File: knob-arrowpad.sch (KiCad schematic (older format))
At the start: 14 parts

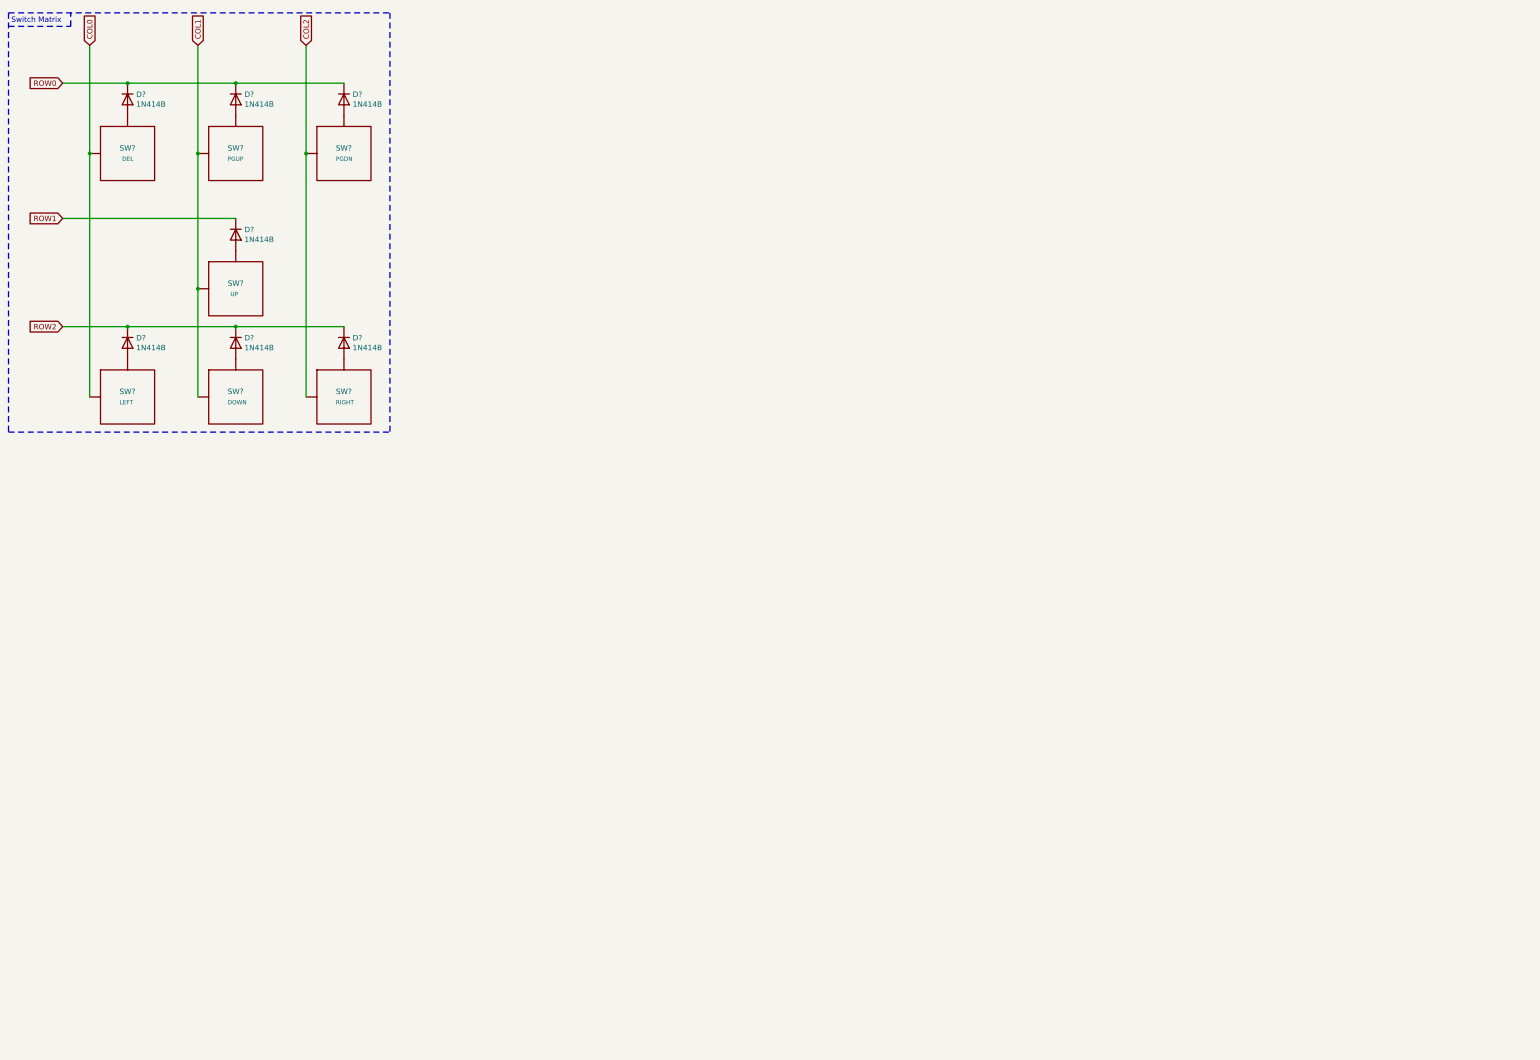
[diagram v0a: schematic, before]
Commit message: Added encoder scematic with filtering and shield
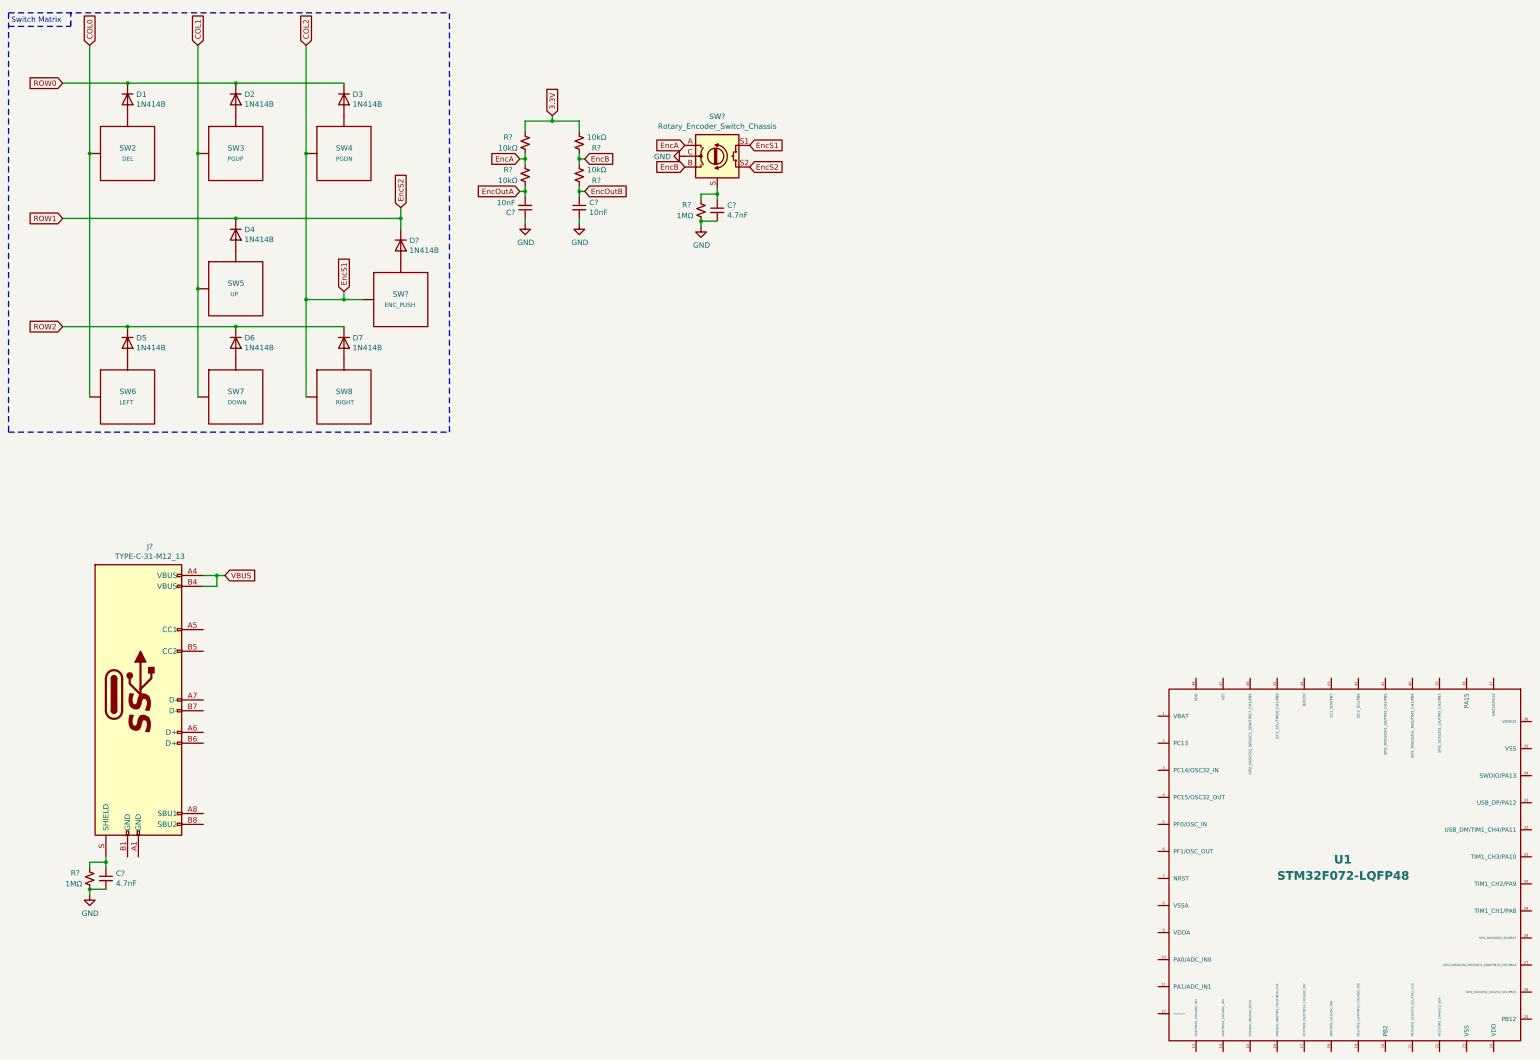
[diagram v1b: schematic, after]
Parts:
- added C? (x2): 4.7nF, symbol Device:C_Small
- added C? (x2): 10nF, symbol Device:C_Small
- added D?: 1N414B, symbol Device:D
- added J?: TYPE-C-31-M12_13, acheronConnectors:TYPE-C-31-M-12, symbol acheronSymbols:TYPE-C-31-M12_13
- added R? (x2): 1MΩ, symbol Device:R_Small_US
- added R? (x4): 10kΩ, symbol Device:R_Small_US
- added SW?: ENC_PUSH, symbol acheronSymbols:MXSwitch
- added SW?: Rotary_Encoder_Switch_Chassis, symbol acheronSymbols:Rotary_Encoder_Switch_Chassis
- added U1: STM32F072-LQFP48, acheron_Components:LQFP-48_7x7mm_P0.5mm, symbol acheronSymbols:STM32F072-LQFP48
- gave numbers to parts that had none: 14
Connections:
- net COL2: now also SW?.1 (Col), SW?.S1
- net ROW1 renamed EncS2
- net EncS2: now also D?.1 (K), SW?.S2
- new net: D?.2 (A), SW?.2 (Row)
- new net: C?.1, J?.S (SHIELD), R?.1
- new net: C?.1, R?.1, SW?.S (Shield)
- new net 3.3V: R?.1, R?.2
- new net EncA: R?.1, R?.2, SW?.A
- new net EncB: R?.1, R?.2, SW?.B
- new net EncOutA: C?.2, R?.2
- new net EncOutB: C?.1, R?.1
- new net GND: C?.1, C?.2, C?.2, C?.2, R?.2, R?.2, SW?.C
- new net VBUS: J?.A4 (VBUS), J?.B4 (VBUS)
